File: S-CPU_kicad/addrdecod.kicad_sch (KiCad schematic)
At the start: 40 parts

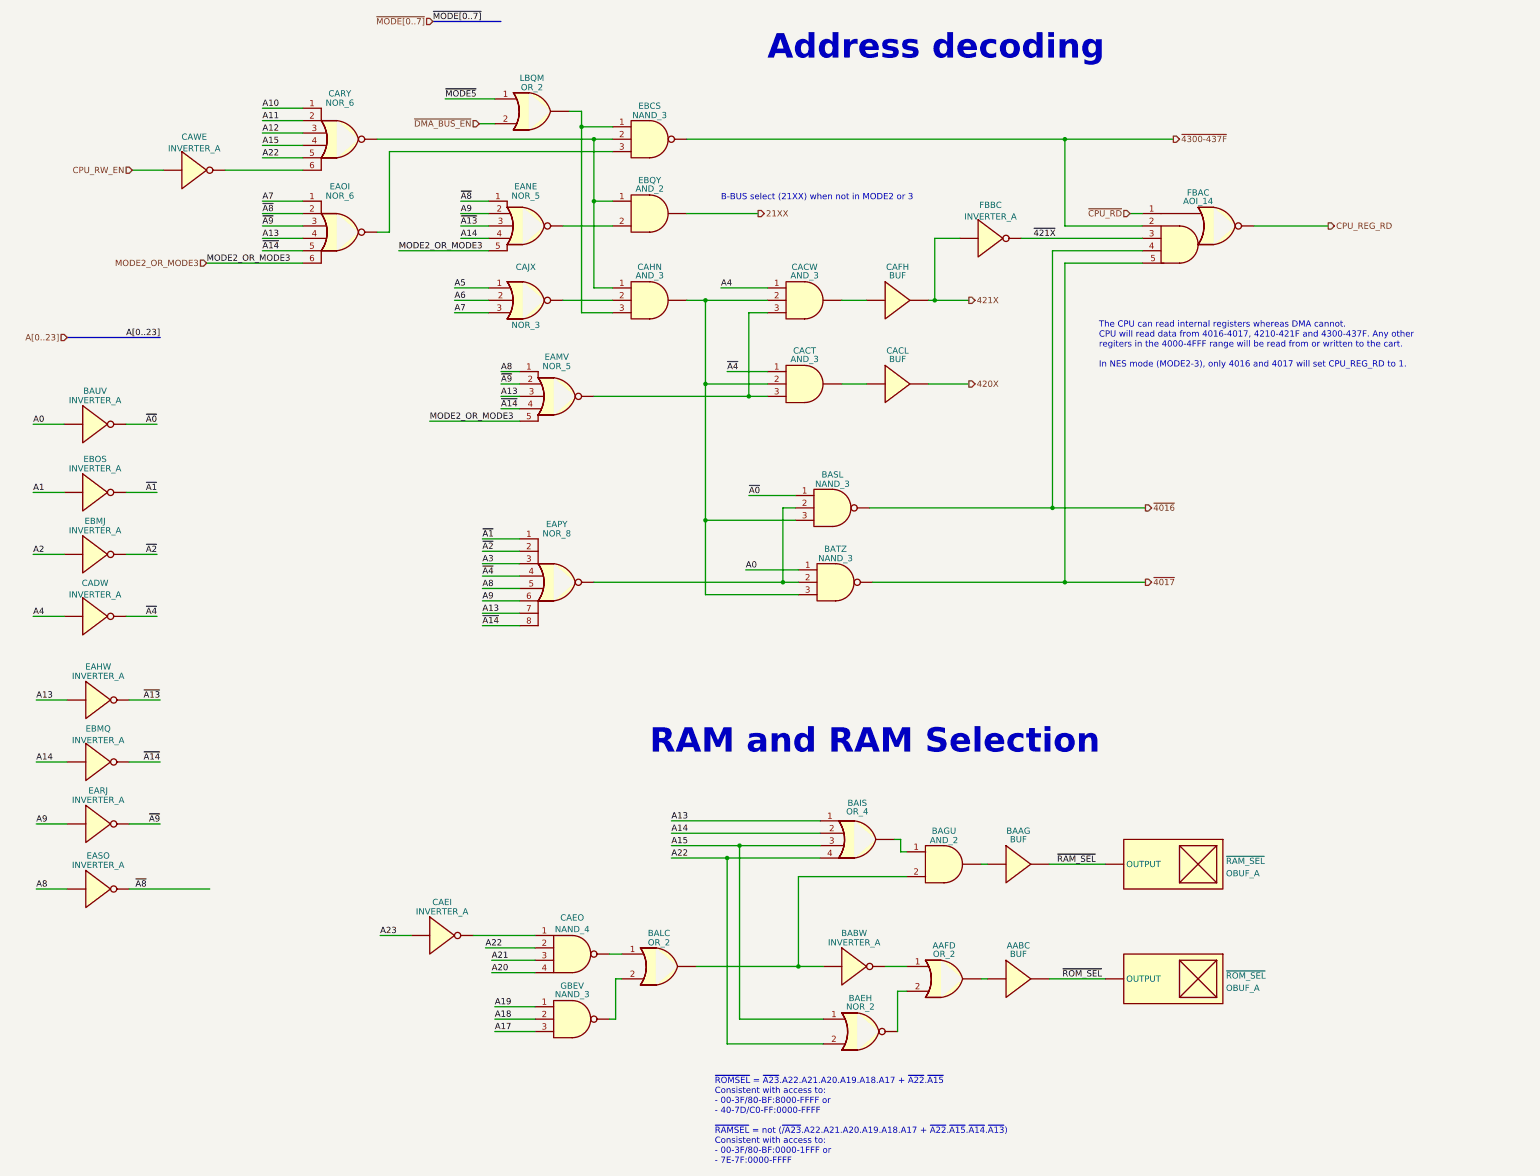
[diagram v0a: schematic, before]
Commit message: Fixed VAWR which should have been an SR DFF (to fix issue #3 raised in github)
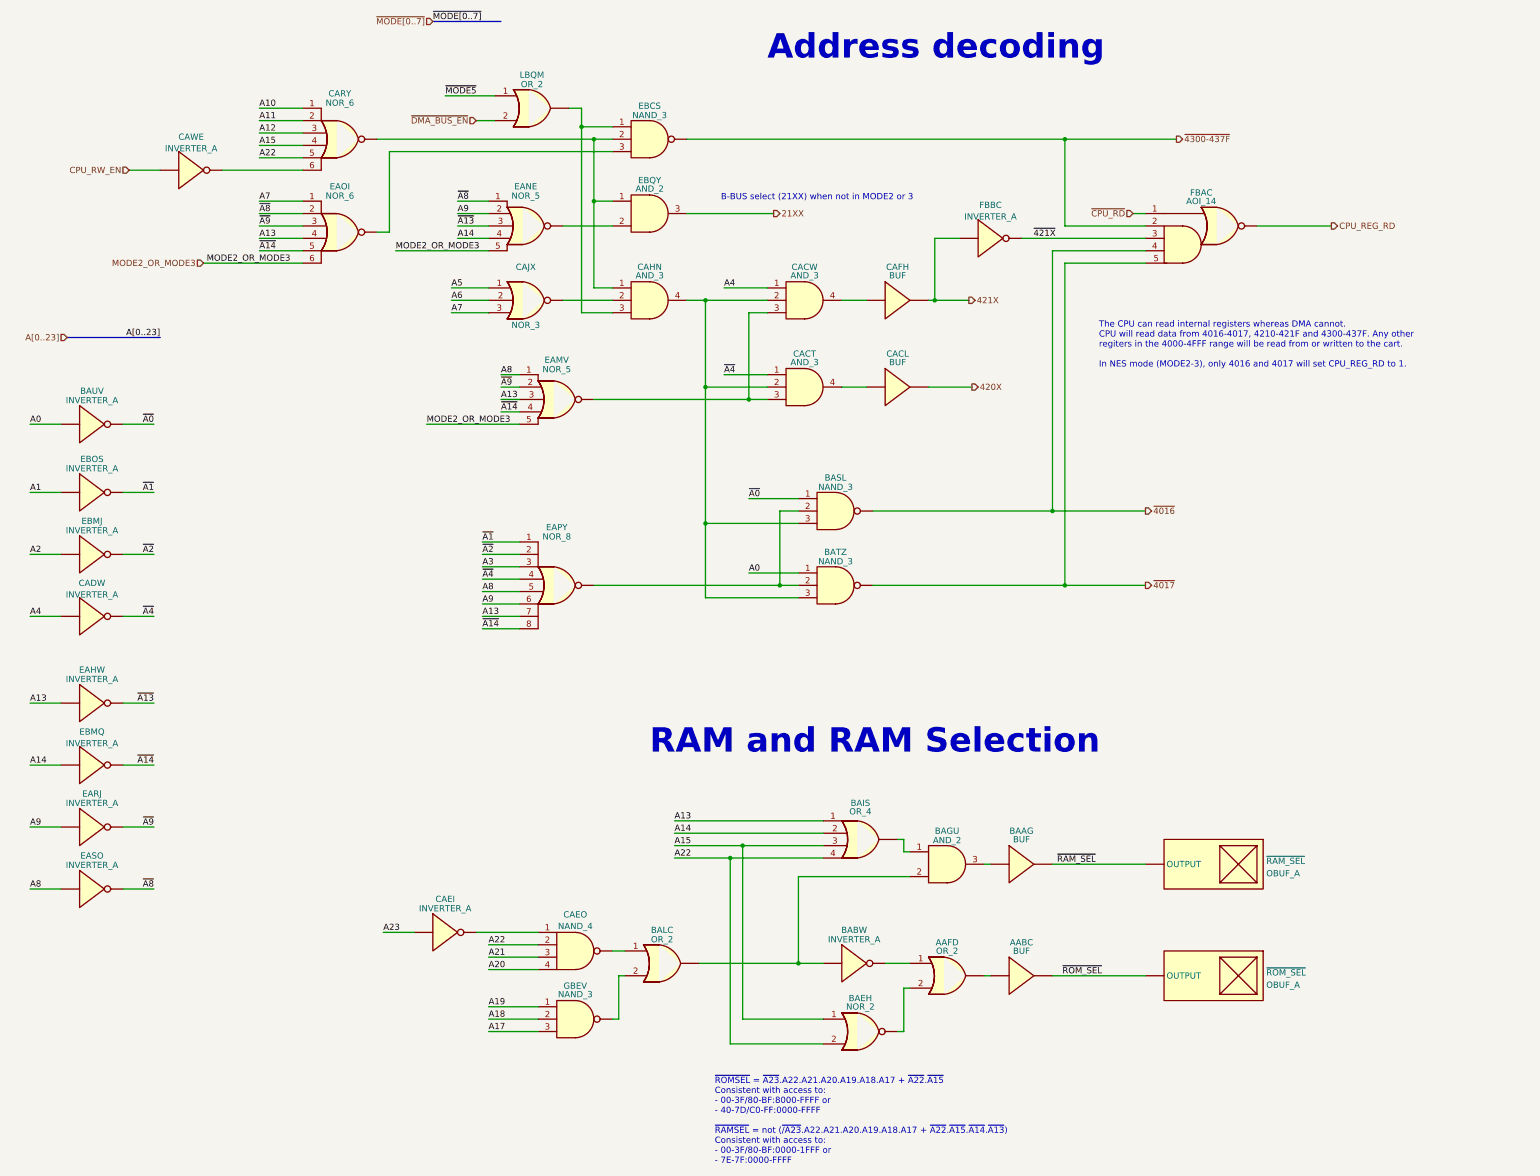
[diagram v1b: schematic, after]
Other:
- moved on the sheet: AABC, AAFD, BAAG, BABW, BAIS, BALC, BASL, BATZ, BAUV, CACL, CADW, CAEI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
